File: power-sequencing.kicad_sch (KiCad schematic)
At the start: 0 parts

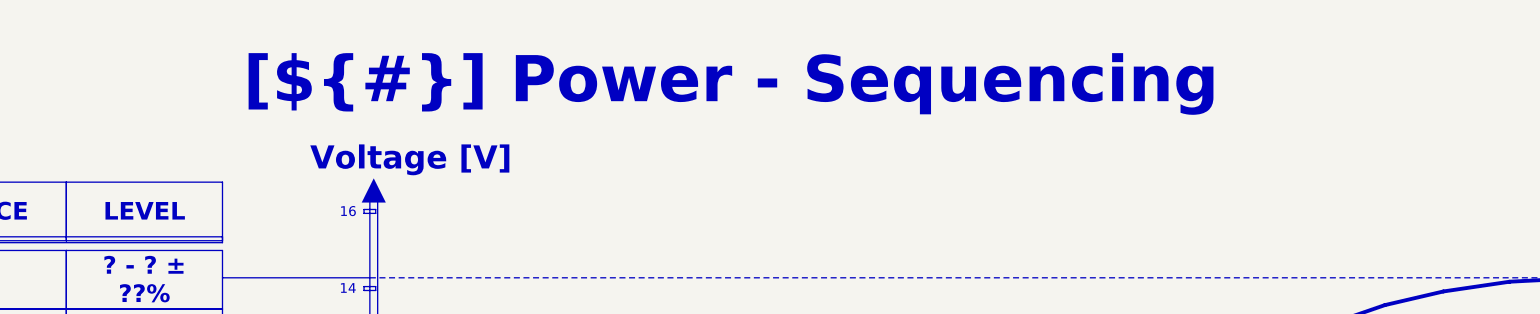
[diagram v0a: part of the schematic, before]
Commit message: feat: convert template to Boardwright
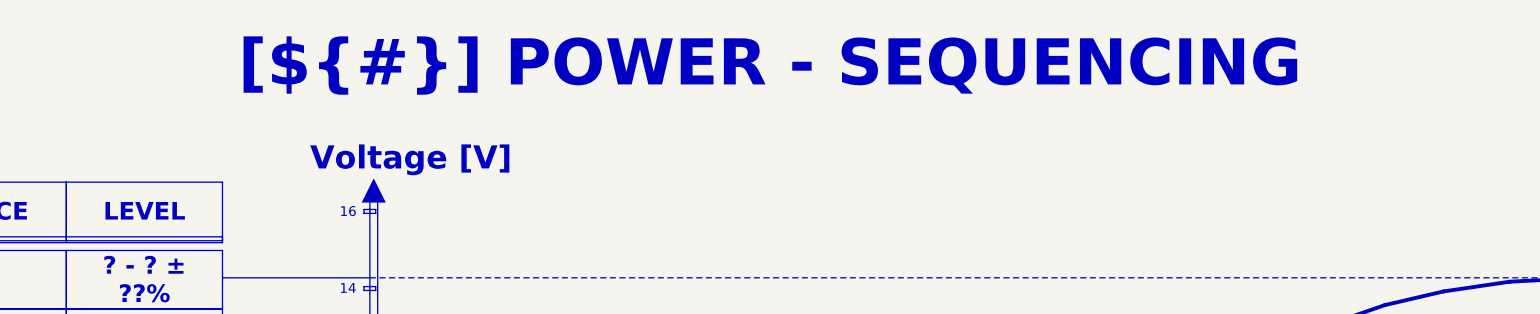
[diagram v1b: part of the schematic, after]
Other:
- title: Power - Sequencing -> POWER - SEQUENCING
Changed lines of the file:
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@@
 	(paper "A4")
 	(title_block
-		(title "Power - Sequencing")
+		(title "POWER - SEQUENCING")
 		(date "2025-01-12")
 		(rev "${REVISION}")
@@
 	(text_box "[${#}] ${TITLE}"
 		(exclude_from_sim no)
-		(at 80.01 15 0)
-		(size 137.16 15)
+		(at 20.32 10.16 0)
+		(size 266.7 20.32)
 		(margins 4.4999 4.4999 4.4999 4.4999)
 		(stroke
